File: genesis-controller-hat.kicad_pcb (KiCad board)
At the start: 2 copper layers, 65 x 56 mm, 5 parts, among them J1 PinSocket_2x20_P2.54mm_Vertic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, J2 DSUB-9_Pins_Horizontal_P2.77x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, J3 DSUB-9_Pins_Horizontal_P2.77x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

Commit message: Fix +3V3 same-layer track crossings, clean up J2/J3 routing -- DRC 0/0
+3V3 crossed 8 other nets on F.Cu on its way from J1 to J2/J3 pin 5
(a real short, not just a DRC nitpick -- kicad-cli was only surfacing
4 of the 8). Rerouted both +3V3 legs to go around the outside of the
J2/J3 pin field instead of weaving between individual pins, entering
pin 5 from clear space beyond the connector rather than crossing the
other GPIO nets' traces. Segment count for +3V3 dropped from 87 to 13.

Verified with kicad-cli pcb drc --refill-zones: 0 violations. The one
remaining "unconnected pad" report is benign and pre-existing -- +3V3
is two disconnected copper islands on this board, but both get power
from the Pi header's own internally-tied +3.3V pins (1 and 17), so it
doesn't need local copper continuity.
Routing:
- net +3V3: track 93.4 -> 142.4 mm
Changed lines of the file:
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@@
 	)
 	(segment
-		(start 154.995 89.46)
-		(end 154.995 80)
+		(start 142.715 89.46)
+		(end 142.715 94.2)
 		(width 0.4)
 		(layer "F.Cu")
@@
 	)
 	(segment
-		(start 120.995 89.46)
-		(end 120.995 80)
-		(width 0.4)
-		(layer "F.Cu")
-		(net "+3V3")
-	)
-	(segment
-		(start 120.995 80)
+		(start 108 49.14)
 		(end 108.37 48.77)
 		(width 0.4)
@@
 	)
 	(segment
-		(start 154.995 80)
+		(start 142.715 89.46)
+		(end 139.96 89.46)
+		(width 0.4)
+		(layer "F.Cu")
+		(net "+3V3")
+	)
+	(segment
+		(start 128.69 78.19)
 		(end 128.69 48.77)
 		(width 0.4)
 		(layer "F.Cu")
+		(net "+3V3")
+	)
+	(segment
+		(start 157.5 94.2)
+		(end 157.5 89.9)
+		(width 0.4)
+		(layer "F.Cu")
+		(net "+3V3")
+	)
+	(segment
+		(start 108 67.005)
+		(end 108 94.2)
+		(width 0.4)
+		(layer "F.Cu")
+		(net "+3V3")
+	)
+	(segment
+		(start 108 67.005)
+		(end 108 49.14)
+		(width 0.4)
+		(layer "F.Cu")
+		(net "+3V3")
+	)
+	(segment
+		(start 108 94.2)
+		(end 123.5 94.2)
+		(width 0.4)
+		(layer "F.Cu")
+		(net "+3V3")
+	)
+	(segment
+		(start 142.715 94.2)
+		(end 157.5 94.2)
+		(width 0.4)
+		(layer "F.Cu")
+		(net "+3V3")
+	)
+	(segment
+		(start 139.96 89.46)
+		(end 128.69 78.19)
+		(width 0.4)
+		(layer "F.Cu")
+		(net "+3V3")
+	)
+	(segment
+		(start 123.5 94.2)
+		(end 123.5 89.9)
+		(width 0.4)
+		(layer "F.Cu")
+		(net "+3V3")
+	)
+	(segment
+		(start 123.5 89.9)
+		(end 120.995 89.46)
+		(width 0.4)
+		(layer "F.Cu")
+		(net "+3V3")
+	)
+	(segment
+		(start 157.5 89.9)
+		(end 154.995 89.46)
+		(width 0.4)
+		(layer "F.Cu")

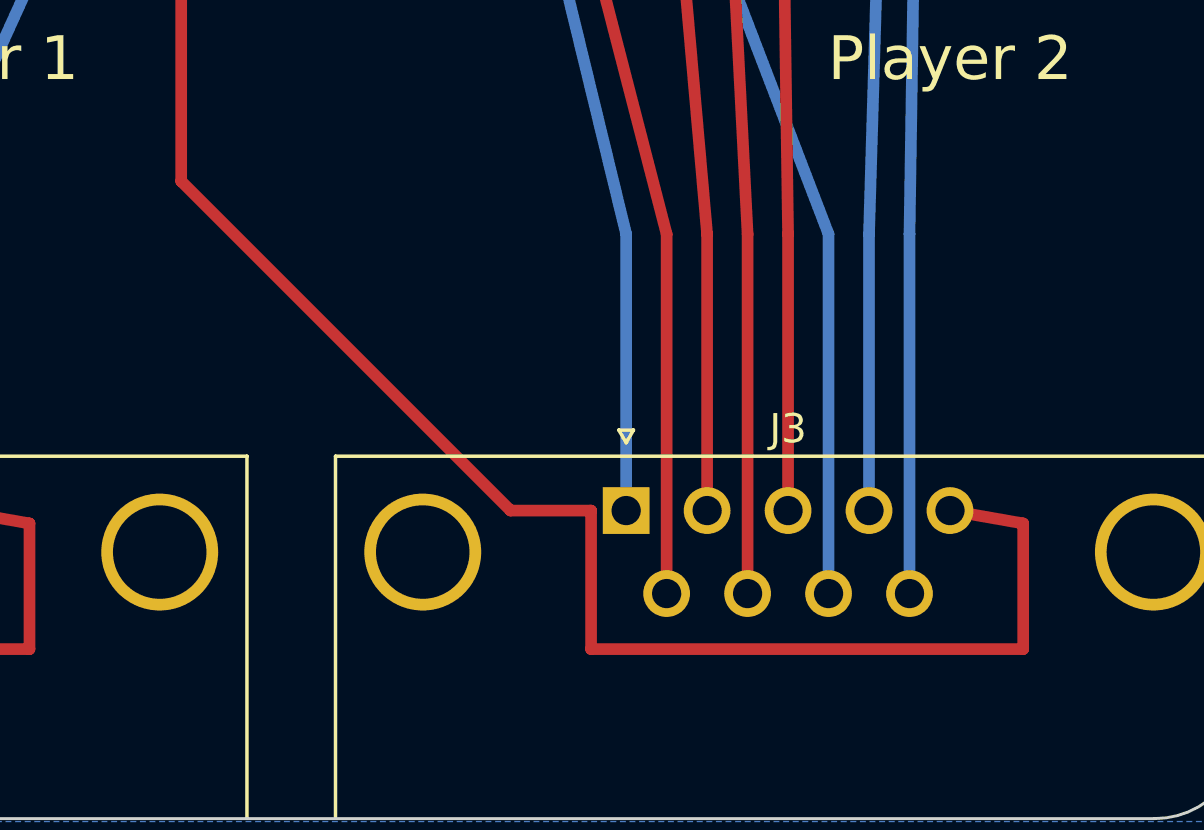
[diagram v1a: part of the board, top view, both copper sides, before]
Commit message: Minor +3V3 jog adjustment near J3
Small tweak to chain B's outside-the-pin-field jog point, made
interactively in the KiCad GUI. DRC unaffected -- still 0 violations.
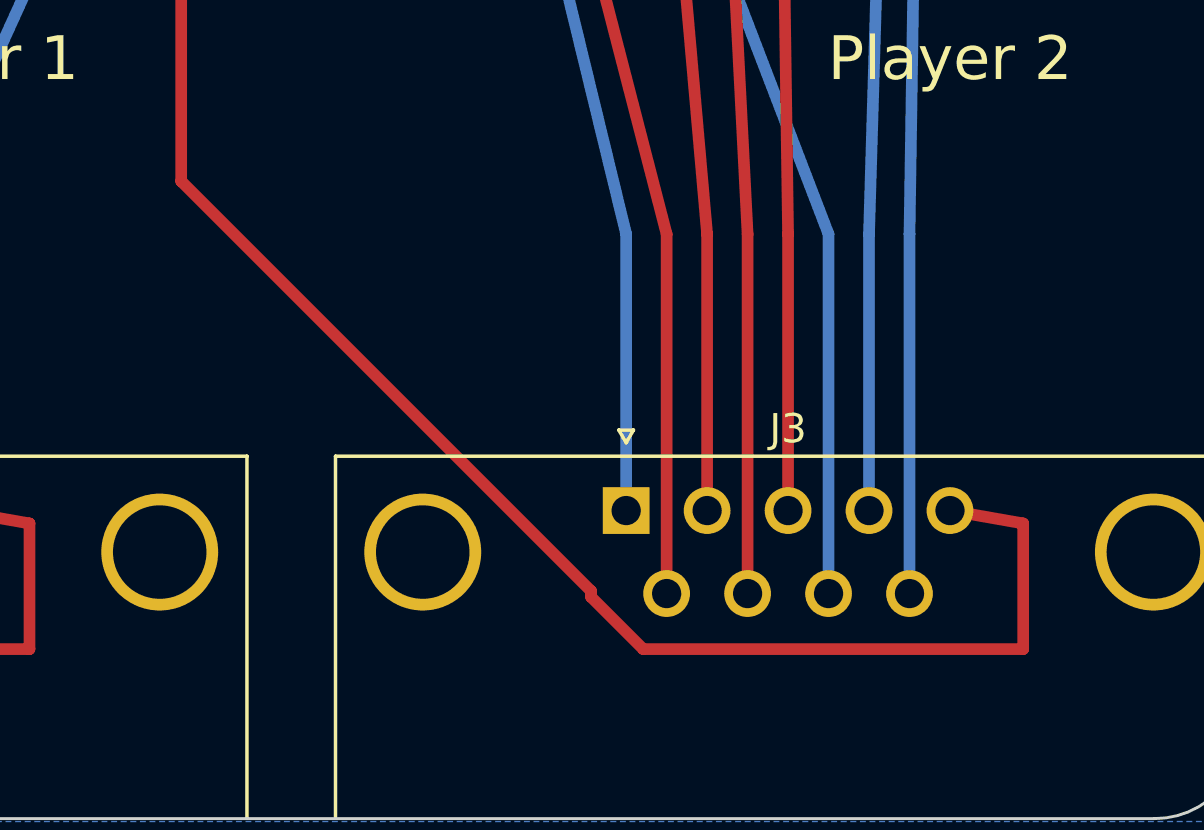
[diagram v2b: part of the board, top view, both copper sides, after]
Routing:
- net +3V3: track 142.4 -> 139.7 mm
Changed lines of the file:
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@@
 	)
 	(segment
-		(start 142.715 89.46)
-		(end 142.715 94.2)
+		(start 157.5 94.2)
+		(end 144.5 94.2)
+		(width 0.4)
+		(layer "F.Cu")
+		(net "+3V3")
+	)
+	(segment
+		(start 157.5 89.9)
+		(end 157.5 94.2)
 		(width 0.4)
 		(layer "F.Cu")
@@
 	)
 	(segment
-		(start 142.715 89.46)
-		(end 139.96 89.46)
-		(width 0.4)
-		(layer "F.Cu")
-		(net "+3V3")
-	)
-	(segment
 		(start 128.69 78.19)
 		(end 128.69 48.77)
-		(width 0.4)
-		(layer "F.Cu")
-		(net "+3V3")
-	)
-	(segment
-		(start 157.5 94.2)
-		(end 157.5 89.9)
 		(width 0.4)
 		(layer "F.Cu")
@@
 	)
 	(segment
+		(start 142.715 92.215)
+		(end 128.69 78.19)
+		(width 0.4)
+		(layer "F.Cu")
+		(net "+3V3")
+	)
+	(segment
 		(start 108 67.005)
 		(end 108 49.14)
+		(width 0.4)
+		(layer "F.Cu")
+		(net "+3V3")
+	)
+	(segment
+		(start 142.715 92.415)
+		(end 142.715 92.215)
 		(width 0.4)
 		(layer "F.Cu")
@@
 	)
 	(segment
-		(start 142.715 94.2)
-		(end 157.5 94.2)
-		(width 0.4)
-		(layer "F.Cu")
-		(net "+3V3")
-	)
-	(segment
-		(start 139.96 89.46)
-		(end 128.69 78.19)
+		(start 144.5 94.2)
+		(end 142.715 92.415)
 		(width 0.4)
 		(layer "F.Cu")
@@
 	)
 	(segment
-		(start 157.5 89.9)
-		(end 154.995 89.46)
+		(start 154.995 89.46)
+		(end 157.5 89.9)
 		(width 0.4)
 		(layer "F.Cu")
